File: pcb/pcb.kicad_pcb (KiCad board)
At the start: 2 copper layers, 33.6 x 27 mm, 44 parts, among them J1 Conn_01x02_Socket, J2 Conn_01x04_Socket, U1 AP2112K-3.3TRG1, U2 W25Q16JVUXIQ, U3 RP2040, U4 DS4432U+T&amp;R, U5 AD8403ARUZ1-REEL, U6 ADG801BRTZ-REEL7, Y2 Crystal_GND24_Small

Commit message: Adjust 3D model position
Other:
- board text removed: "v1.0"

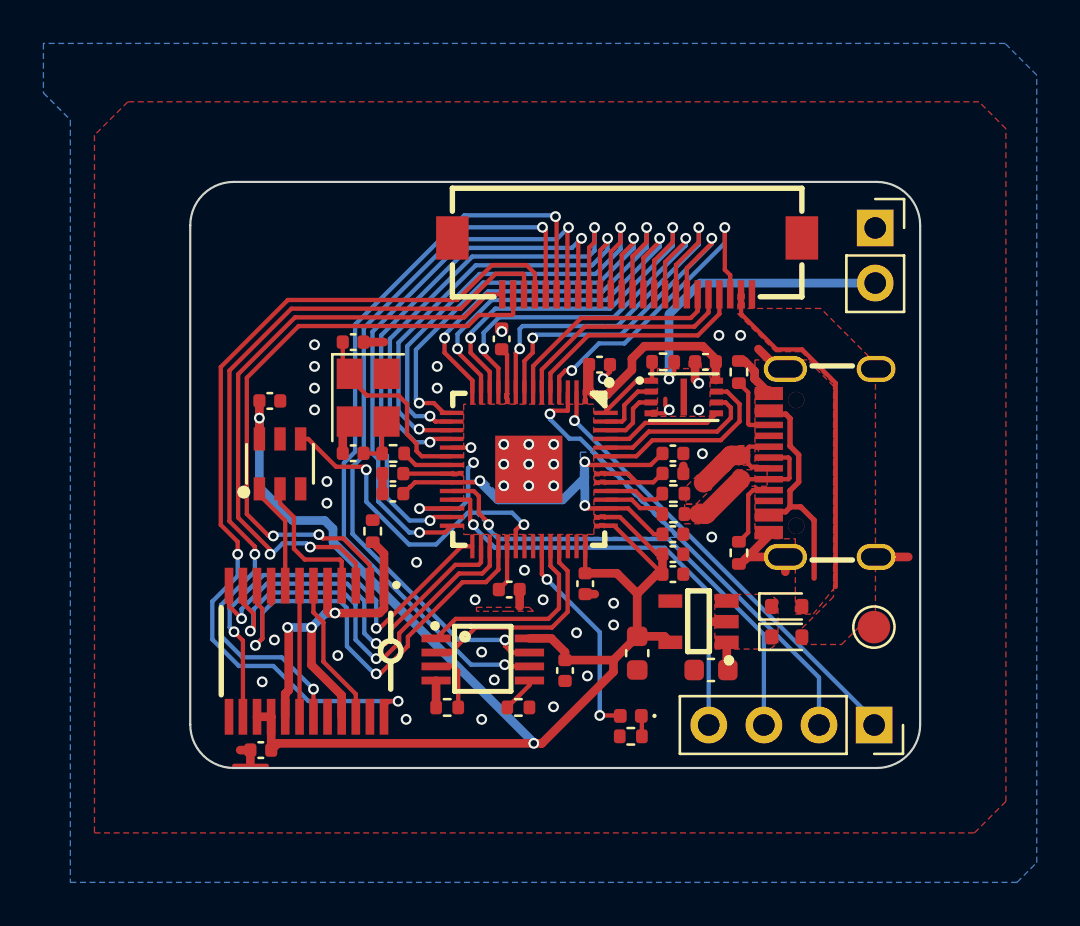
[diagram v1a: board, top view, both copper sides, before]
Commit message: Type-C connector stick out as much as possible
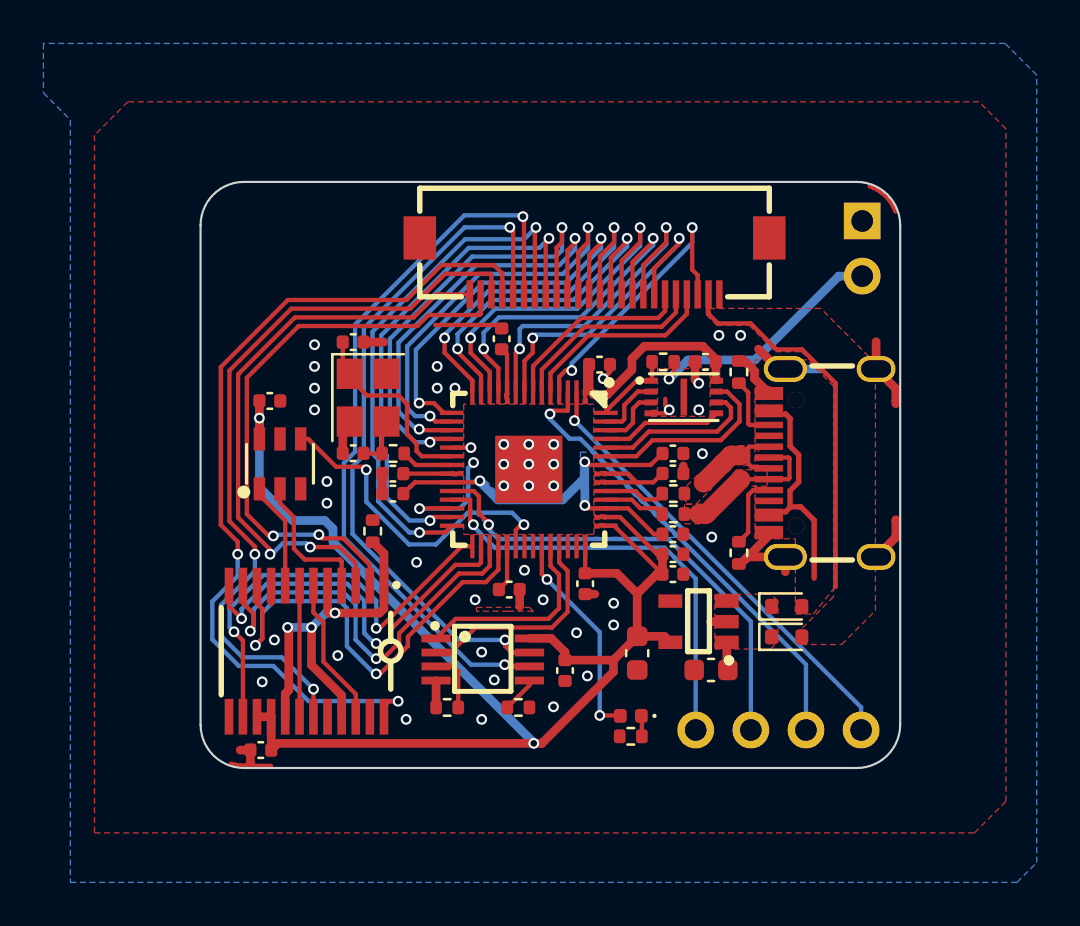
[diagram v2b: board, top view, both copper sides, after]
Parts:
- removed TP1: TestPoint, TestPoint:TestPoint_Pad_D1.5mm
- moved FPC1 1.50 mm to (123.0, 53.9)
- moved J1 0.68 mm to (135.3, 51.8)
- moved J2 0.64 mm to (135.3, 75.2)
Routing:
- net GND: track 25.3 -> 36.1 mm
- net Net-(J1-Pin_2): track 14.0 -> 11.8 mm
- net 3DS_TP86_X: track 10.6 -> 9.08 mm
- net 3DS_TP85_UP: track 21.1 -> 19.6 mm
- net 3DS_TP83_L: track 16.0 -> 14.5 mm
- net 3DS_TP52_POWER: track 18.4 -> 16.9 mm
- net 3DS_TP91_DOWN: track 22.3 -> 20.8 mm
- net 3DS_TP90_RIGHT: track 20.6 -> 19.1 mm
- net 3DS_TP80_START: track 18.3 -> 16.8 mm
- net 3DS_TP58_WIFI: track 19.4 -> 17.9 mm
- net 3DS_TP55_HOME: track 17.4 -> 15.9 mm
- net 3DS_TP82_R: track 17.2 -> 15.6 mm
- net 3DS_TP81_SELECT: track 17.6 -> 16.1 mm
- net 3DS_TP213_X-: track 36.2 -> 34.7 mm
- net 3DS_TP214_Y-: track 28.2 -> 26.7 mm
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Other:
- board size 33.6 x 27 mm -> 32.2 x 27 mm

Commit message: Adjust FPC connector slightly to the left
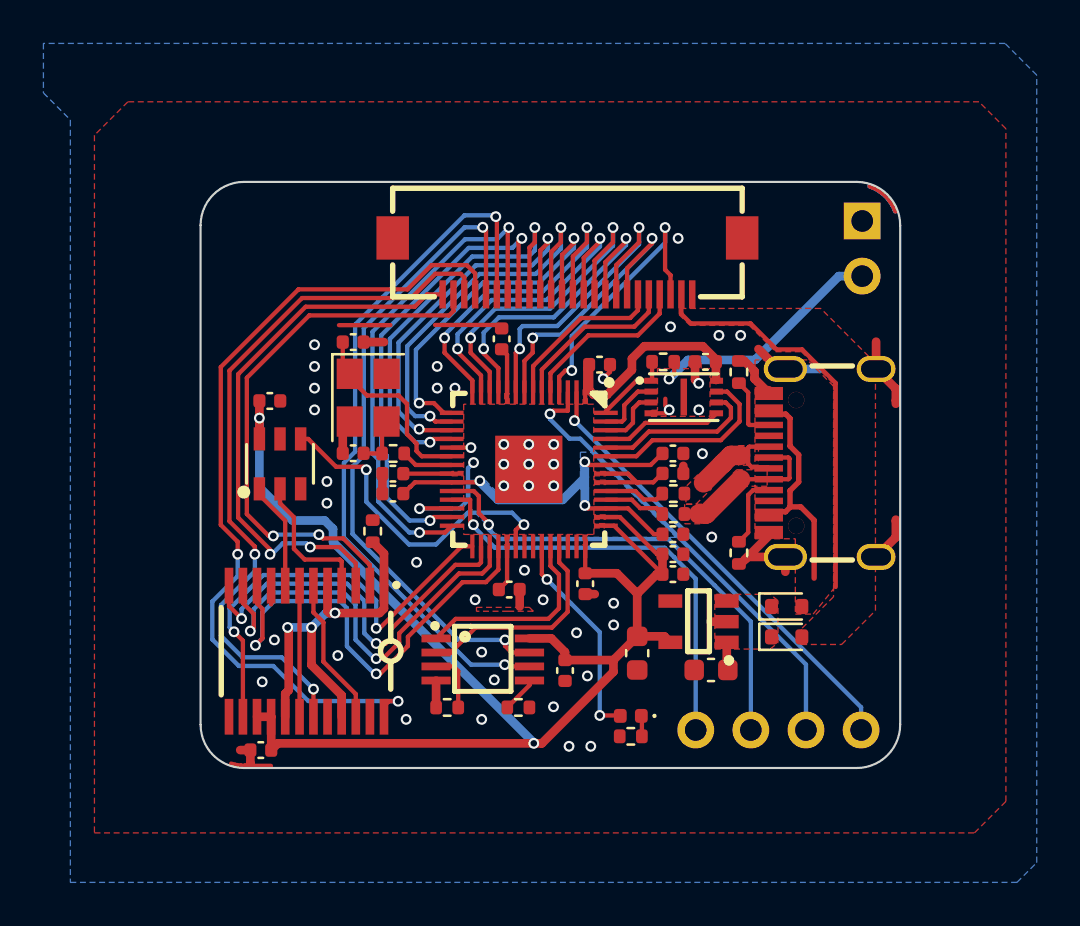
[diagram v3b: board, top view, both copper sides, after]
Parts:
- moved FPC1 1.25 mm to (121.8, 53.9)
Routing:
- net GND: track 36.1 -> 40.2 mm, vias 43 -> 47
- net 3DS_TP216_Y+: track 26.8 -> 25.5 mm
- net 3DS_TP213_X-: track 34.7 -> 33.4 mm
- net 3DS_TP92_B: track 9.21 -> 7.93 mm
- net 3DS_TP89_A: track 9.16 -> 7.89 mm
- net 3DS_TP215_X+: track 40.4 -> 39.1 mm
- net 3DS_TP214_Y-: track 26.7 -> 25.4 mm
- net 3DS_TP32_5V: track 17.5 -> 18.7 mm
- net 3DS_TP80_START: track 16.8 -> 15.6 mm
- net 3DS_TP91_DOWN: track 20.8 -> 19.6 mm
- net 3DS_TP90_RIGHT: track 19.1 -> 17.9 mm
- net 3DS_TP87_LEFT: track 23.3 -> 22.1 mm
- net 3DS_TP85_UP: track 19.6 -> 18.3 mm
- net 3DS_TP83_L: track 14.5 -> 13.3 mm
- net 3DS_TP82_R: track 15.6 -> 14.4 mm
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
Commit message: Add GND via
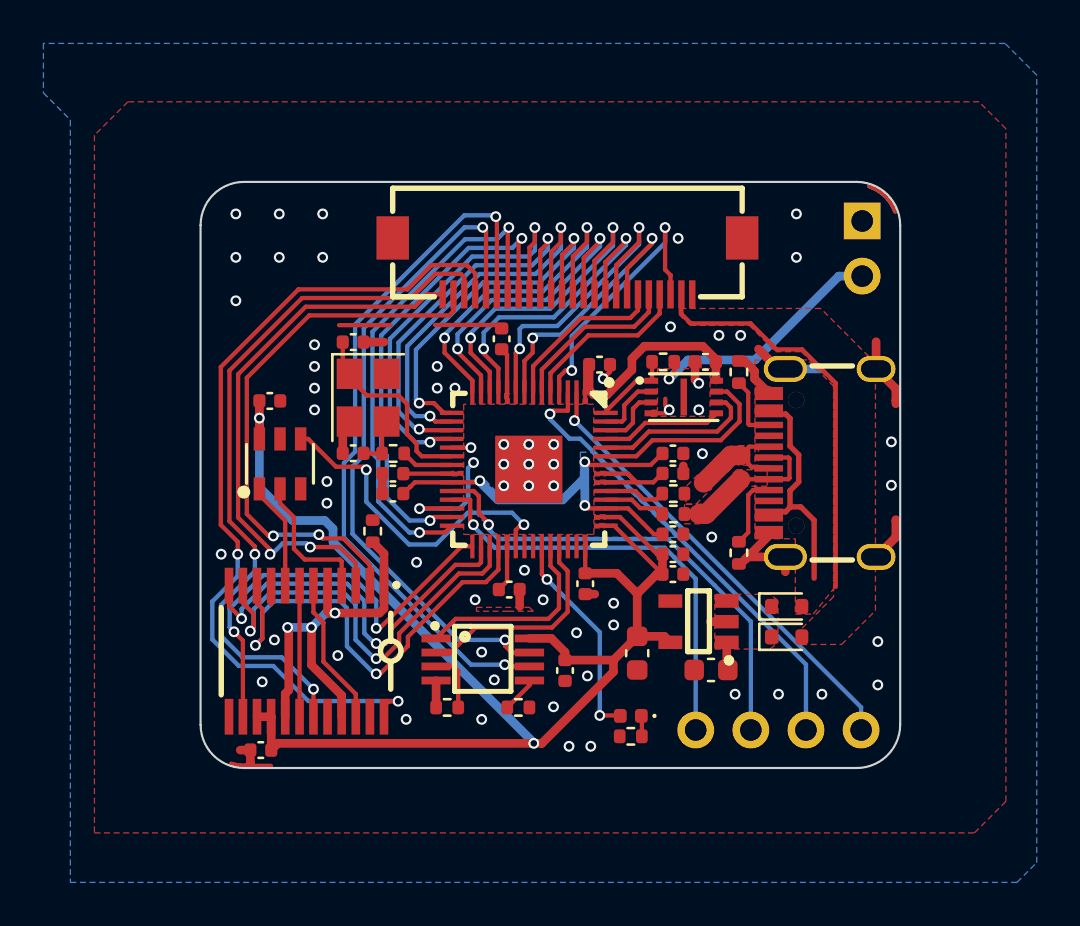
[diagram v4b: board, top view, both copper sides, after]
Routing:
- net GND: vias 47 -> 64

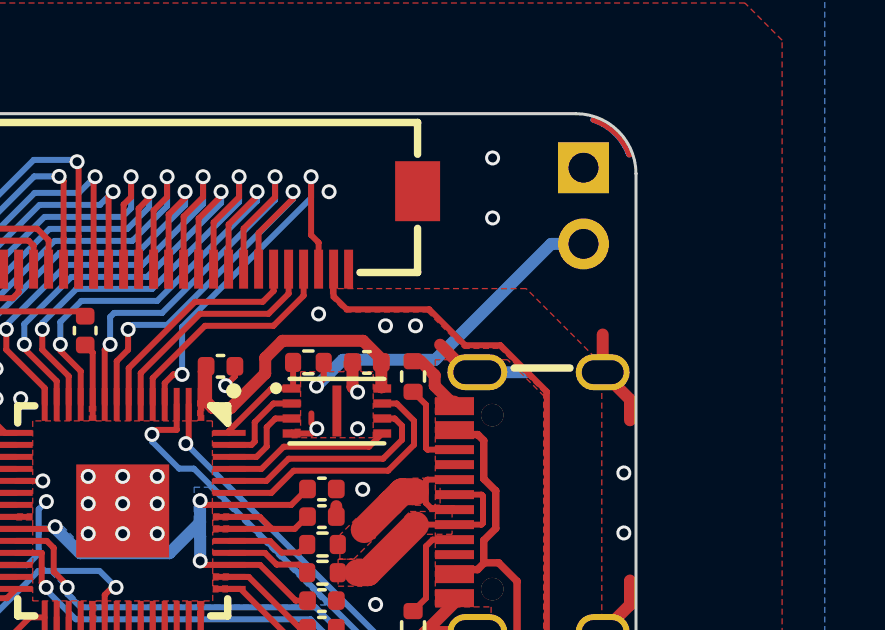
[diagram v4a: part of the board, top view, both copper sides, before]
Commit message: Tweak BOOTSEL path
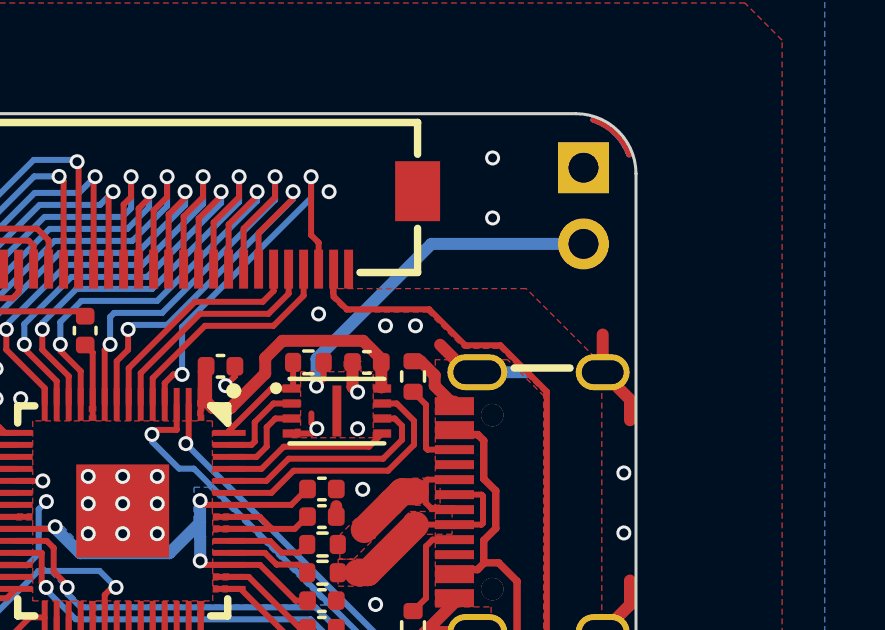
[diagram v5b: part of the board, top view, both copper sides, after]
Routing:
- net Net-(J1-Pin_2): track 11.8 -> 12.3 mm

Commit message: Add URL on silkscreen
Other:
- board text added: "https://github.com/ U-1F992/NeoCtrlMod"
